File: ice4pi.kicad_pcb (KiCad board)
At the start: 4 copper layers, 85 x 56 mm, 33 parts, among them J1 Conn_02x03, J2 Raspberry_Pi_2_3, J3 USB_C_Receptacle_USB2.0, J5 RJ45_Abracon_ARJP11A-MASA-B-A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, U1 ENC28J60x-SS, U2 DSC1001DE1-025.0000

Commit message: feat: poe controller
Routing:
- net Net-(J3-CC1): track 3.38 -> 7.83 mm
- net Net-(J5-TCT): track 21.0 -> 19.8 mm
- net +3.3V: track 27.0 -> 26.2 mm
- net GND: vias 9 -> 7
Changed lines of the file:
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@@
 		(tags "capacitor")
 		(property "Reference" "C9"
-			(at 0 -1.16 360)
+			(at 0 -1.16 0)
 			(layer "F.SilkS")
 			(effects
@@
 		)
 		(property "Value" "100 nF"
-			(at 0 1.16 360)
+			(at 0 1.16 0)
 			(layer "F.Fab")
 			(effects
@@
 		)
 		(fp_text user "${REFERENCE}"
-			(at 0 0 360)
+			(at 0 0 0)
 			(layer "F.Fab")
 			(effects
@@
 		(tags "resistor")
 		(property "Reference" "R3"
-			(at 0 -1.17 360)
+			(at 0 -1.17 0)
 			(layer "F.SilkS")
 			(effects
@@
 		)
 		(property "Value" "50"
-			(at 0 1.17 360)
+			(at 0 1.17 0)
 			(layer "F.Fab")
 			(effects
@@
 		)
 		(fp_text user "${REFERENCE}"
-			(at 0 0 360)
+			(at 0 0 0)
 			(layer "F.Fab")
 			(effects
@@
 	)
 	(via
-		(at 116.8 66.1)
-		(size 0.8)
-		(drill 0.4)
-		(layers "F.Cu" "B.Cu")
-		(free yes)
-		(net 1)
-	)
-	(via
 		(at 115.7 86.9)
 		(size 0.8)
@@
 	)
 	(via
-		(at 120.7 73.2)
-		(size 0.8)
-		(drill 0.4)
-		(layers "F.Cu" "B.Cu")
-		(free yes)
-		(net 1)
-	)
-	(via
 		(at 92.3418 66.2466)
 		(size 0.8)
@@
 	)
 	(segment
+		(start 128.1 74.085728)
+		(end 128.221383 74.207111)
+		(width 0.2)
+		(layer "F.Cu")
+		(net 2)
+	)
+	(segment
 		(start 124.825 89.175)
 		(end 124.5 89.5)
@@
 	)
 	(segment
+		(start 128.1 74)
+		(end 128.1 74.085728)
+		(width 0.2)
+		(layer "F.Cu")
+		(net 2)
+	)
+	(segment
 		(start 132.12 88.48)
 		(end 131.775 88.825)
@@
 	)
 	(segment
-		(start 128.1 74)
-		(end 128.1 75)
-		(width 0.2)
-		(layer "F.Cu")
-		(net 2)
-	)
-	(segment
 		(start 128 92.38)
 		(end 129.08 92.38)
@@
 	)
 	(via
-		(at 128.1 75)
+		(at 128.221383 74.207111)
 		(size 0.8)
 		(drill 0.4)
@@
 	)
 	(segment
+		(start 62.825 99.62)
+		(end 62.95 99.495)
+		(width 0.25)
+		(layer "F.Cu")
+		(net 32)
+	)
+	(segment
+		(start 59.95 98.82)
+		(end 59.95 99.495)
+		(width 0.25)
+		(layer "F.Cu")
+		(net 32)
+	)
+	(segment
 		(start 62.95 98.82)
 		(end 62.95 95.64)
@@
 	)
 	(segment
+		(start 59.95 99.495)
+		(end 60.075 99.62)
+		(width 0.25)
+		(layer "F.Cu")
+		(net 32)
+	)
+	(segment
+		(start 62.95 99.495)
+		(end 62.95 98.82)
+		(width 0.25)
+		(layer "F.Cu")
+		(net 32)
+	)
+	(segment
 		(start 62.95 95.64)
 		(end 63.09 95.5)
@@
 	)
 	(segment
+		(start 60.075 99.62)
+		(end 62.825 99.62)
+		(width 0.25)
+		(layer "F.Cu")
+		(net 32)
+	)
+	(segment
 		(start 115.78 79.68)
 		(end 114.8 78.7)
@@
 	)
 	(segment
-		(start 128.1 69.82)
-		(end 128.08 69.8)
+		(start 128.221383 71.407111)
+		(end 128.1 71.285728)
 		(width 0.2)
 		(layer "F.Cu")
@@
 	)
 	(segment
-		(start 128.1 71.2)
-		(end 128.1 69.82)
+		(start 126.22 71.2)
+		(end 126.11 71.31)
 		(width 0.2)
 		(layer "F.Cu")
@@
 	)
 	(segment
-		(start 128.1 71.2)
-		(end 128.1 72.4)
+		(start 128.1 71.285728)
+		(end 128.1 69.82)
 		(width 0.2)
 		(layer "F.Cu")
@@
 	(segment
 		(start 126.22 71.2)
-		(end 126.11 71.31)
+		(end 126.427111 71.407111)
 		(width 0.2)
 		(layer "F.Cu")
@@
 	)
 	(segment
-		(start 126.22 71.2)
-		(end 126.427111 71.407111)
+		(start 126.11 71.31)
+		(end 126.11 70.8)
 		(width 0.2)
 		(layer "F.Cu")
@@
 	)
 	(segment
-		(start 126.11 71.31)
-		(end 126.11 70.8)
+		(start 128.1 69.82)
+		(end 128.08 69.8)
 		(width 0.2)
 		(layer "F.Cu")
@@
 	)
 	(via
-		(at 128.1 72.4)
+		(at 128.221383 71.407111)
 		(size 0.8)
 		(drill 0.4)
@@
 	)
 	(segment
-		(start 126.790836 72.4)
-		(end 122 67.609164)
+		(start 122 62.655)
+		(end 120.5 61.155)
 		(width 0.2)
 		(layer "B.Cu")
@@
 	)
 	(segment
-		(start 122 67.609164)
-		(end 122 62.655)
+		(start 128.221383 71.407111)
+		(end 125.797947 71.407111)
 		(width 0.2)
 		(layer "B.Cu")
@@
 	)
 	(segment
-		(start 122 62.655)
-		(end 120.5 61.155)
+		(start 122 67.609164)
+		(end 122 62.655)
 		(width 0.2)
 		(layer "B.Cu")
@@
 	)
 	(segment
-		(start 128.1 72.4)
-		(end 126.790836 72.4)
+		(start 125.797947 71.407111)
+		(end 122 67.609164)
 		(width 0.2)
 		(layer "B.Cu")

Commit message: feat: finished poe-1.0
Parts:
- added C15: 100nF 100V, Capacitor_SMD:C_0402_1005Metric, F.Cu at (106.5, 98.5)
- added D4: SMAJ58A, Diode_SMD:D_SMA, F.Cu at (104.0, 88.5)
- added R22: 24.9K, Resistor_SMD:R_0402_1005Metric, F.Cu at (106.5, 96.0)
- added R23: 180K, Resistor_SMD:R_0402_1005Metric, F.Cu at (106.5, 92.5)
- added R24: 4.42K, Resistor_SMD:R_0402_1005Metric, F.Cu at (107.5, 92.5)
- added U3: TPS2375-1, Package_SO:TSSOP-8_4.4x3mm_P0.65mm, F.Cu at (104.0, 96.9)
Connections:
- LSI-U1 pad 1: POE_V- -> GND
- LSI-U1 pad 5: GND -> unconnected-(LSI-U1-S1-Pad5)
- LSI-U1 pad 6: unconnected-(LSI-U1-S2-Pad6) -> Net-(LSI-U1-S2)
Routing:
- net POE_V+: track 54.4 -> 96.0 mm, vias 3 -> 4
- net POE_V-: track 57.4 -> 72.1 mm, vias 4 -> 6
- net Net-(LSI-U1-S2): track 0.00 -> 13.4 mm
- net GND: track 13.2 -> 22.2 mm, vias 7 -> 9
- net Net-(U3-CLASS): track 0.00 -> 4.79 mm
- net Net-(U3-DET): track 0.00 -> 3.85 mm
- net Net-(U3-ILIM): track 0.00 -> 1.91 mm

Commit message: feat: finished poe-1.0
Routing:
- net GND: track 22.2 -> 22.7 mm, vias 9 -> 11
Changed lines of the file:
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@@
 	)
 	(gr_text "ethernet4pizero-poe-1.0"
-		(at 86 104 0)
+		(at 82 57.5 0)
 		(layer "F.SilkS")
 		(effects
@@
 	)
 	(segment
+		(start 73.8 88.7)
+		(end 73.5 89)
+		(width 2)
+		(layer "F.Cu")
+		(net 1)
+	)
+	(segment
+		(start 73.5 97)
+		(end 73.8 97.3)
+		(width 2)
+		(layer "F.Cu")
+		(net 1)
+	)
+	(segment
+		(start 73.8 89.3)
+		(end 73.8 96.7)
+		(width 2)
+		(layer "F.Cu")
+		(net 1)
+	)
+	(segment
 		(start 73.8 88)
-		(end 73.8 97.9)
+		(end 73.8 88.7)
+		(width 2)
+		(layer "F.Cu")
+		(net 1)
+	)
+	(segment
+		(start 73.5 89)
+		(end 73.8 89.3)
 		(width 2)
 		(layer "F.Cu")
@@
 		(net 1)
 	)
+	(segment
+		(start 73.8 96.7)
+		(end 73.5 97)
+		(width 2)
+		(layer "F.Cu")
+		(net 1)
+	)
+	(segment
+		(start 73.8 97.3)
+		(end 73.8 97.9)
+		(width 2)
+		(layer "F.Cu")
+		(net 1)
+	)
+	(via
+		(at 73.5 89)
+		(size 0.8)
+		(drill 0.4)
+		(layers "F.Cu" "B.Cu")
+		(net 1)
+	)
 	(via
 		(at 94.958 63.6558)
@@
 		(net 1)
 	)
+	(via
+		(at 73.5 97)
+		(size 0.8)
+		(drill 0.4)
+		(layers "F.Cu" "B.Cu")
+		(net 1)
+	)

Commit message: feat: finished poe-1.0
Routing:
- net POE_V-: track 72.1 -> 73.7 mm
- net GND: track 22.7 -> 23.6 mm
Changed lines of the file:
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@@
 	)
 	(segment
-		(start 73.8 88.7)
-		(end 73.5 89)
+		(start 73.8 96)
+		(end 73.8 97.9)
 		(width 2)
 		(layer "F.Cu")
@@
 	)
 	(segment
-		(start 73.5 97)
-		(end 73.8 97.3)
+		(start 73.8 88)
+		(end 73.8 90)
 		(width 2)
 		(layer "F.Cu")
@@
 	)
 	(segment
-		(start 73.8 88)
-		(end 73.8 88.7)
-		(width 2)
-		(layer "F.Cu")
-		(net 1)
-	)
-	(segment
-		(start 73.5 89)
-		(end 73.8 89.3)
-		(width 2)
-		(layer "F.Cu")
-		(net 1)
-	)
-	(segment
 		(start 126.3 88.525)
 		(end 127.805 88.525)
@@
 		(net 1)
 	)
-	(segment
-		(start 73.8 96.7)
-		(end 73.5 97)
-		(width 2)
-		(layer "F.Cu")
-		(net 1)
-	)
-	(segment
-		(start 73.8 97.3)
-		(end 73.8 97.9)
-		(width 2)
-		(layer "F.Cu")
-		(net 1)
-	)
-	(via
-		(at 73.5 89)
+	(via
+		(at 73.8 89)
 		(size 0.8)
 		(drill 0.4)
@@
 	)
 	(via
-		(at 73.5 97)
+		(at 73.8 97)
 		(size 0.8)
 		(drill 0.4)
@@
 	)
 	(via
-		(at 98.5 74)
+		(at 99.25 73.25)
 		(size 0.8)
 		(drill 0.4)
@@
 	)
 	(segment
-		(start 91.4 89)
-		(end 91.4 81)
+		(start 91.4 81)
+		(end 91.4 89)
 		(width 1)
 		(layer "In1.Cu")
@@
 	)
 	(segment
-		(start 98.4 74)
-		(end 98.5 74)
+		(start 99.25 73.25)
+		(end 99.15 73.25)
 		(width 1)
 		(layer "In1.Cu")
@@
 	)
 	(segment
-		(start 91.4 81)
-		(end 98.4 74)
+		(start 99.15 73.25)
+		(end 91.4 81)
 		(width 1)
 		(layer "In1.Cu")
@@
 	)
 	(segment
-		(start 98.5 74)
+		(start 99.25 73.25)
 		(end 104 68.5)
 		(width 1)
@@
 	)
 	(segment
-		(start 120.5 53.535)
-		(end 120.27 53.305)
-		(width 1)
-		(layer "F.Cu")
-		(net 51)
-	)
-	(segment
 		(start 107.49 92)
 		(end 107.5 91.99)
@@
 	)
 	(segment
+		(start 119.6 52.635)
+		(end 120.5 53.535)
+		(width 1)
+		(layer "F.Cu")
+		(net 51)
+	)
+	(segment
 		(start 105 90.5)
 		(end 106.5 92)
@@
 	)
 	(segment
+		(start 115.5 55)
+		(end 102.5 68)
+		(width 1)
+		(layer "F.Cu")
+		(net 51)
+	)
+	(segment
 		(start 104 90.5)
 		(end 105 90.5)
@@
 	)
 	(segment
-		(start 117.195 53.305)
-		(end 102.5 68)
-		(width 1)
-		(layer "F.Cu")
-		(net 51)
-	)
-	(segment
 		(start 107 98)
 		(end 106.5 98)
@@
 	)
 	(segment
-		(start 120.27 53.305)
-		(end 117.195 53.305)
+		(start 116.17 52.635)
+		(end 119.6 52.635)
 		(width 1)
 		(layer "F.Cu")
+		(net 51)
+	)
+	(segment
+		(start 115.5 53.305)
+		(end 115.5 55)
+		(width 1)
+		(layer "F.Cu")
+		(net 51)
+	)
+	(segment
+		(start 115.5 53.305)
+		(end 116.17 52.635)
+		(width 1)
+		(layer "F.Cu")

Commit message: fix: added resistor
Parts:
- added R6: 5.1K, Resistor_SMD:R_0402_1005Metric, F.Cu at (59.5, 95.5)
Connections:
- J3 pad B5: Net-(J3-CC1) -> Net-(J3-CC2)
- R9 pad 1: Net-(J3-CC1) -> Net-(J3-CC2)
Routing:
- net Net-(J3-CC1): track 7.83 -> 3.34 mm
- net Net-(J3-CC2): track 0.00 -> 3.38 mm
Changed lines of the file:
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@@
 	(net 67 "Net-(U3-CLASS)")
 	(net 68 "unconnected-(U3-NC-Pad7)")
+	(net 69 "Net-(J3-CC2)")
 	(footprint "ice4pi:mount_hole"
 		(locked yes)
@@
 			(layers "F.Cu" "F.Paste" "F.Mask")
 			(roundrect_rratio 0.25)
-			(net 32 "Net-(J3-CC1)")
+			(net 69 "Net-(J3-CC2)")
 			(pintype "passive")
 		)
@@
 			(size 0.3 1.15)
 			(layers "F.Cu" "F.Paste" "F.Mask")
-			(net 32 "Net-(J3-CC1)")
+			(net 69 "Net-(J3-CC2)")
 			(pinfunction "CC2")
 			(pintype "bidirectional")
@@
 	(footprint "Resistor_SMD:R_0402_1005Metric"
 		(layer "F.Cu")
+		(at 59.49 95.5 180)
+		(descr "Resistor SMD 0402 (1005 Metric), square (rectangular) end terminal, IPC_7351 nominal, (Body size source: IPC-SM-782 page 72, https://www.pcb-3d.com/wordpress/wp-content/uploads/ipc-sm-782a_amendment_1_and_2.pdf), generated with kicad-footprint-generator")
+		(tags "resistor")
+		(property "Reference" "R6"
+			(at 0 -1.17 360)
+			(layer "F.SilkS")
+			(effects
+				(font
+					(size 1 1)
+					(thickness 0.15)
+				)
+			)
+		)
+		(property "Value" "5.1K"
+			(at 0 1.17 360)
+			(layer "F.Fab")
+			(effects
+				(font
+					(size 1 1)
+					(thickness 0.15)
+				)
+			)
+		)
+		(property "Footprint" "Resistor_SMD:R_0402_1005Metric"
+			(at 0 0 180)
+			(unlocked yes)
+			(layer "F.Fab")
+			(hide yes)
+			(effects
+				(font
+					(size 1.27 1.27)
+					(thickness 0.15)
+				)
+			)
+		)
+		(property "Datasheet" ""
+			(at 0 0 180)
+			(unlocked yes)
+			(layer "F.Fab")
+			(hide yes)
+			(effects
+				(font
+					(size 1.27 1.27)
+					(thickness 0.15)
+				)
+			)
+		)
+		(property "Description" ""
+			(at 0 0 180)
+			(unlocked yes)
+			(layer "F.Fab")
+			(hide yes)
+			(effects
+				(font
+					(size 1.27 1.27)
+					(thickness 0.15)
+				)
+			)
+		)
+		(property ki_fp_filters "R_*")
+		(sheetname "Root")
+		(sheetfile "ice4pi.kicad_sch")
+		(attr smd)
+		(fp_line
+			(start -0.153641 0.38)
+			(end 0.153641 0.38)
+			(stroke
+				(width 0.12)
+				(type solid)
+			)
+			(layer "F.SilkS")
+		)
+		(fp_line
+			(start -0.153641 -0.38)
+			(end 0.153641 -0.38)
+			(stroke
+				(width 0.12)
+				(type solid)
+			)
+			(layer "F.SilkS")
+		)
+		(fp_line
+			(start 0.93 0.47)
+			(end -0.93 0.47)
+			(stroke
+				(width 0.05)
+				(type solid)
+			)
+			(layer "F.CrtYd")
+		)
+		(fp_line
+			(start 0.93 -0.47)
+			(end 0.93 0.47)
+			(stroke
+				(width 0.05)
+				(type solid)
+			)
+			(layer "F.CrtYd")
+		)
+		(fp_line
+			(start -0.93 0.47)
+			(end -0.93 -0.47)
+			(stroke
+				(width 0.05)
+				(type solid)
+			)
+			(layer "F.CrtYd")
+		)
+		(fp_line
+			(start -0.93 -0.47)
+			(end 0.93 -0.47)
+			(stroke
+				(width 0.05)
+				(type solid)
+			)
+			(layer "F.CrtYd")
+		)
+		(fp_line
+			(start 0.525 0.27)
+			(end -0.525 0.27)
+			(stroke
+				(width 0.1)
+				(type solid)
+			)
+			(layer "F.Fab")
+		)
+		(fp_line
+			(start 0.525 -0.27)
+			(end 0.525 0.27)
+			(stroke
+				(width 0.1)
+				(type solid)
+			)
+			(layer "F.Fab")
+		)
+		(fp_line
+			(start -0.525 0.27)
+			(end -0.525 -0.27)
+			(stroke
+				(width 0.1)
+				(type solid)
+			)
+			(layer "F.Fab")
+		)
+		(fp_line
+			(start -0.525 -0.27)
+			(end 0.525 -0.27)
+			(stroke
+				(width 0.1)
+				(type solid)
+			)
+			(layer "F.Fab")
+		)
+		(fp_text user "${REFERENCE}"
+			(at 0 0 360)
+			(layer "F.Fab")
+			(effects
+				(font
+					(size 0.26 0.26)
+					(thickness 0.04)
+				)
+			)
+		)
+		(pad "1" smd roundrect
+			(at -0.51 0 180)
+			(size 0.54 0.64)
+			(layers "F.Cu" "F.Paste" "F.Mask")
+			(roundrect_rratio 0.25)
+			(net 32 "Net-(J3-CC1)")
+			(pintype "passive")
+		)
+		(pad "2" smd roundrect
+			(at 0.51 0 180)
+			(size 0.54 0.64)
+			(layers "F.Cu" "F.Paste" "F.Mask")
+			(roundrect_rratio 0.25)
+			(net 1 "GND")
+			(pintype "passive")
+		)
+		(model "${KICAD8_3DMODEL_DIR}/Resistor_SMD.3dshapes/R_0402_1005Metric.wrl"
+			(offset
+				(xyz 0 0 0)
+			)
+			(scale
+				(xyz 1 1 1)
+			)
+			(rotate
+				(xyz 0 0 0)
+			)
+		)
+	)
+	(footprint "Resistor_SMD:R_0402_1005Metric"
+		(layer "F.Cu")
 		(at 125.6 70.8 180)
 		(descr "Resistor SMD 0402 (1005 Metric), square (rectangular) end terminal, IPC_7351 nominal, (Body size source: IPC-SM-782 page 72, https://www.pcb-3d.com/wordpress/wp-content/uploads/ipc-sm-782a_amendment_1_and_2.pdf), generated with kicad-footprint-generator")
@@
 	)
 	(segment
-		(start 62.825 99.62)
-		(end 62.95 99.495)
+		(start 60 95.88)
+		(end 60 95.5)
 		(width 0.25)
 		(layer "F.Cu")
@@
 	)
 	(segment
-		(start 59.95 98.82)
-		(end 59.95 99.495)
+		(start 59.95 95.93)
+		(end 60 95.88)
 		(width 0.25)
 		(layer "F.Cu")
@@
 	)
 	(segment
-		(start 62.95 98.82)
-		(end 62.95 95.64)
-		(width 0.2)
-		(layer "F.Cu")
-		(net 32)
-	)
-	(segment
-		(start 59.95 99.495)
-		(end 60.075 99.62)
-		(width 0.25)
-		(layer "F.Cu")
-		(net 32)
-	)
-	(segment
-		(start 62.95 99.495)
-		(end 62.95 98.82)
-		(width 0.25)
-		(layer "F.Cu")
-		(net 32)
-	)
-	(segment
-		(start 62.95 95.64)
-		(end 63.09 95.5)
-		(width 0.2)
-		(layer "F.Cu")
-		(net 32)
-	)
-	(segment
-		(start 60.075 99.62)
-		(end 62.825 99.62)
+		(start 59.95 98.82)
+		(end 59.95 95.93)
 		(width 0.25)
 		(layer "F.Cu")
@@
 		(net 67)
 	)
+	(segment
+		(start 62.95 98.82)
+		(end 62.95 95.64)
+		(width 0.2)
+		(layer "F.Cu")
+		(net 69)
+	)
+	(segment
+		(start 62.95 95.64)
+		(end 63.09 95.5)
+		(width 0.2)
+		(layer "F.Cu")
+		(net 69)
+	)
 	(zone

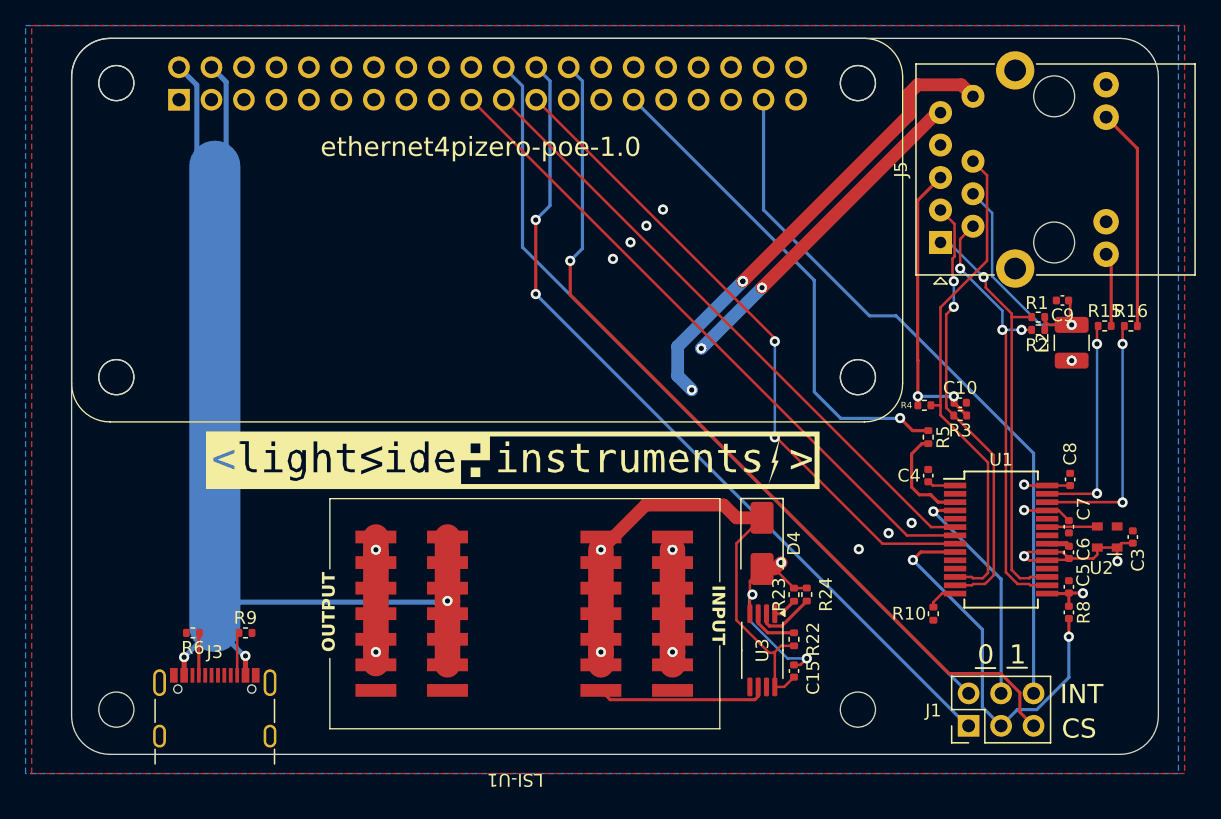
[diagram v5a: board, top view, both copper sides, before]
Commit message: fix: poe_v- trace width
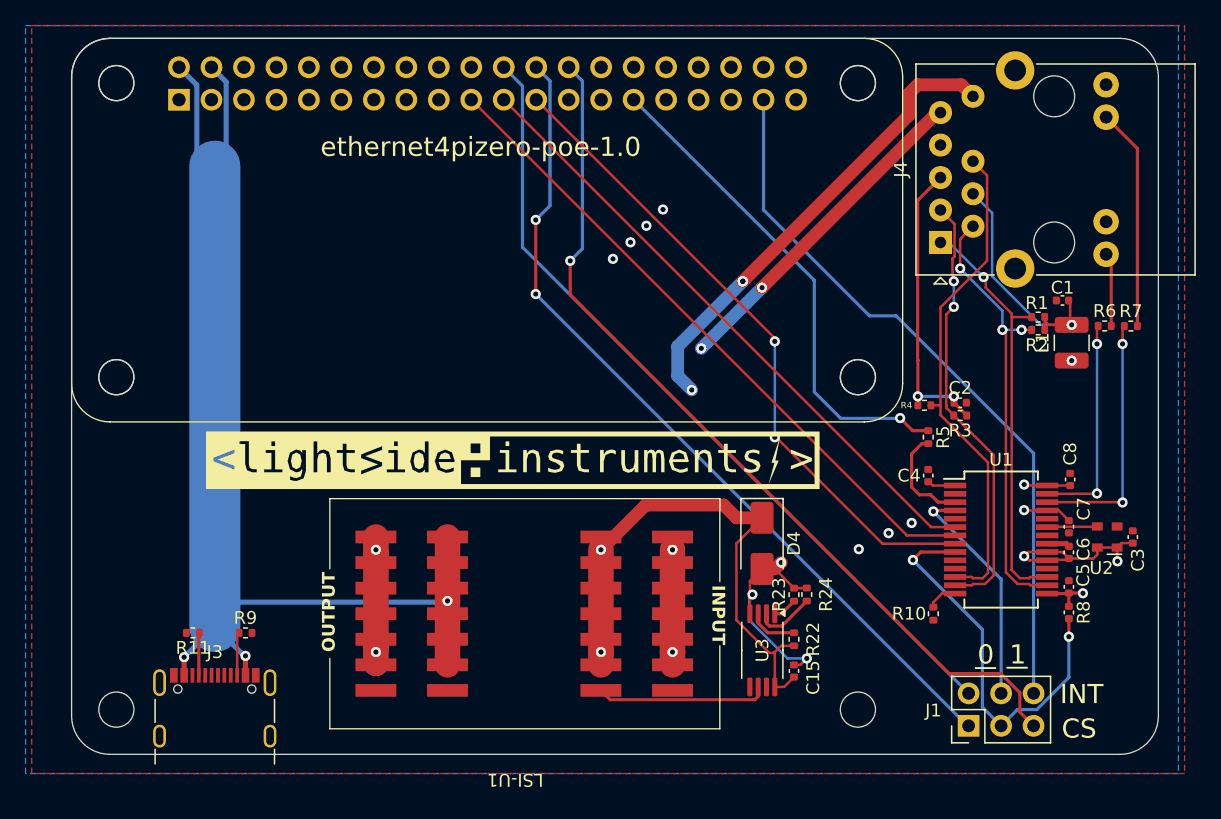
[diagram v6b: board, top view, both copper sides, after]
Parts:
- renumbered C9 to C1, C10 to C2, J5 to J4, L2 to L1, R6 to R11, R15 to R6, R16 to R7
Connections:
- J4 pad 11: Net-(J5-Pad11) -> Net-(J4-Pad11)
- J4 pad 13: Net-(J5-Pad13) -> Net-(J4-Pad13)
- R6 pad 1: /LEDA -> /LEDB
- R6 pad 2: Net-(J5-Pad11) -> Net-(J4-Pad13)
- R7 pad 1: /LEDB -> /LEDA
- R7 pad 2: Net-(J5-Pad13) -> Net-(J4-Pad11)
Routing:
- net (no net): track 0.00 -> 23.1 mm
- net Net-(J5-Pad13): track 17.3 -> 0.00 mm
- net Net-(J5-Pad11): track 5.77 -> 0.00 mm
